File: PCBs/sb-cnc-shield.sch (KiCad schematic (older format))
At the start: 68 parts, among them J8 display, P1 XMOT, P10 power switch, P2 YMOT, P3 ZMOT, P4 AMOT, P5 UART, P6 I2C, P7 E_STOP, P8 12V-36V, Q0 IRF630, SW1 RESET, U1 ARDUINO_UNO_SHIELD, U2 X, U3 Y, U4 Z, U5 A

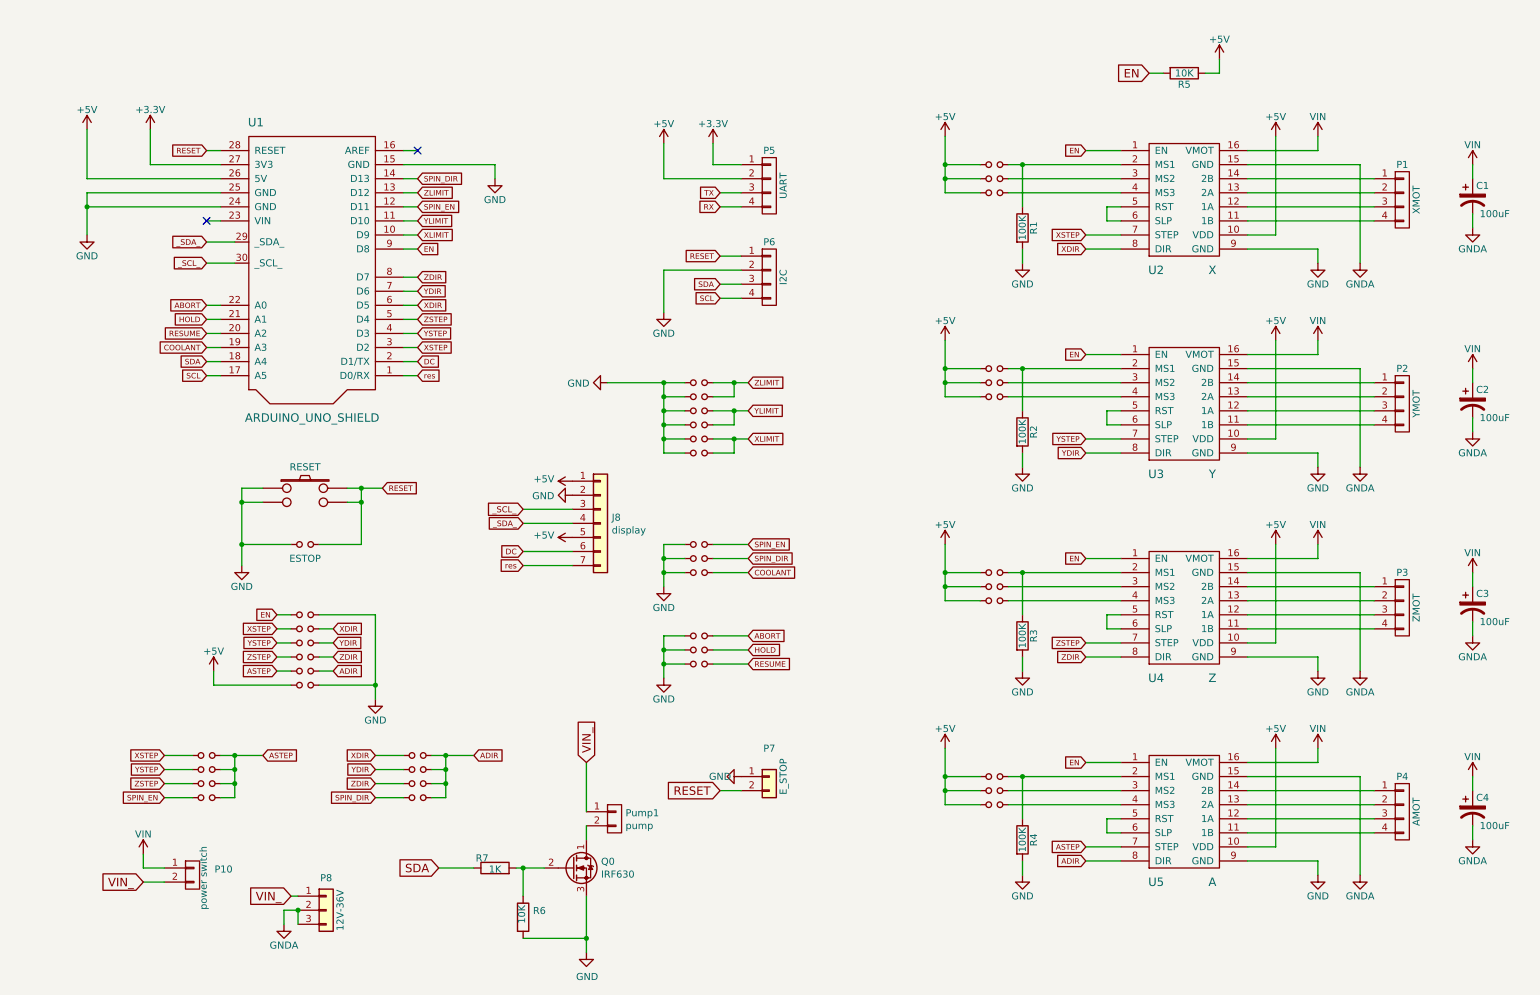
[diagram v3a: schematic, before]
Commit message: add voltage regulator shield for 5V rpi
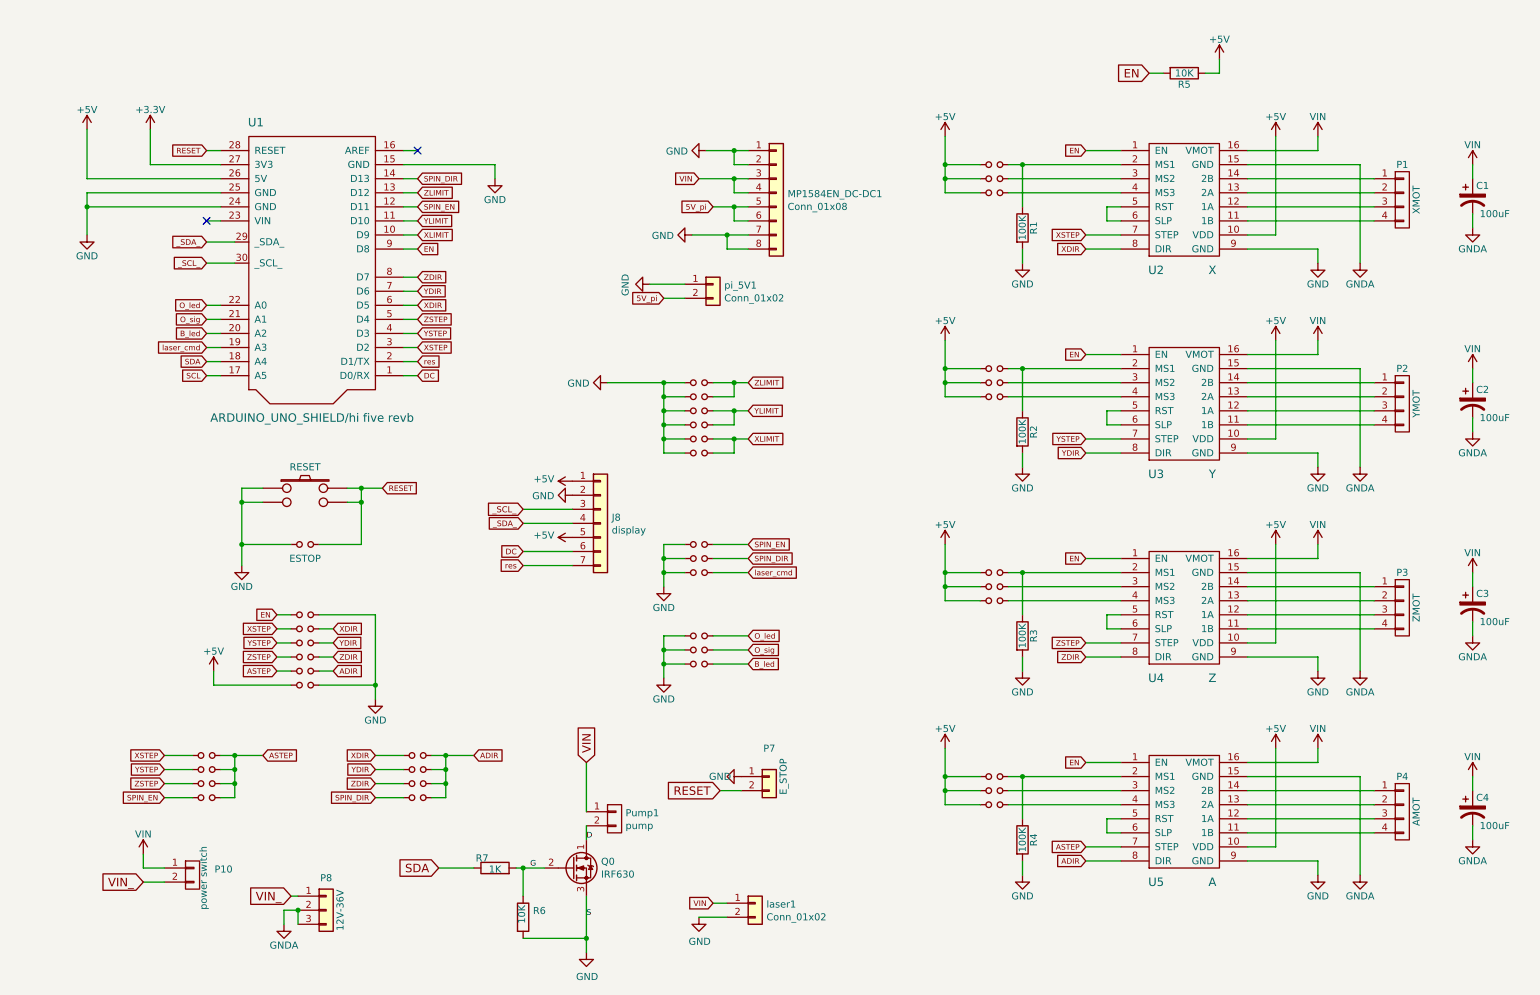
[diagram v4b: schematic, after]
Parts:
- removed P5: UART, Pin_Headers:Pin_Header_Straight_1x04, symbol sb-cnc-shield-rescue:CONN_01X04
- removed P6: I2C, Pin_Headers:Pin_Header_Straight_1x04, symbol sb-cnc-shield-rescue:CONN_01X04
- added MP1584EN_DC-DC1: Conn_01x08, pnp_box:MP1584EN convertisseur DC-DC, symbol Connector_Generic:Conn_01x08
- added laser1: Conn_01x02, Connector_PinHeader_2.54mm:PinHeader_1x02_P2.54mm_Vertical, symbol Connector_Generic:Conn_01x02
- added pi_5V1: Conn_01x02, Connector_JST:JST_EH_S2B-EH_1x02_P2.50mm_Horizontal, symbol Connector_Generic:Conn_01x02
- J8: footprint (none) -> Connector_PinHeader_2.54mm:PinHeader_1x07_P2.54mm_Vertical
- JP21: value CoolEn -> laser_cmd
- JP22: value Abort -> O_led
- JP23: value Hold -> O_sig
- JP24: value Resume -> B_led
- P1, P2, P3, P4: footprint Pin_Headers:Pin_Header_Straight_2x04 -> Connector_PinHeader_2.54mm:PinHeader_1x04_P2.54mm_Vertical
- U1: value ARDUINO_UNO_SHIELD -> ARDUINO_UNO_SHIELD/hi five revb
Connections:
- net DC: now also U1.1 (D0/RX); no longer U1.2 (D1/TX)
- net GND: now also MP1584EN_DC-DC1.1 (Pin_1), MP1584EN_DC-DC1.2 (Pin_2), MP1584EN_DC-DC1.7 (Pin_7), MP1584EN_DC-DC1.8 (Pin_8), laser1.2 (Pin_2), pi_5V1.1 (Pin_1)
- net VIN: now also Pump1.1 (P1), MP1584EN_DC-DC1.3 (Pin_3), MP1584EN_DC-DC1.4 (Pin_4), laser1.1 (Pin_1)
- net VIN_: no longer Pump1.1 (P1)
- net res: now also U1.2 (D1/TX); no longer U1.1 (D0/RX)
- net D: now reaches Pump1.2 (P2), Q0.1 (D)
- net G: now reaches Q0.2 (G), R6.1, R7.2
- net ABORT renamed O_led
- net COOLANT renamed laser_cmd
- net HOLD renamed O_sig
- net RESUME renamed B_led
- new net 5V_pi: MP1584EN_DC-DC1.5 (Pin_5), MP1584EN_DC-DC1.6 (Pin_6), pi_5V1.2 (Pin_2)

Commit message: modify kicad and create gerbers then ordering PCBs on JLPCB
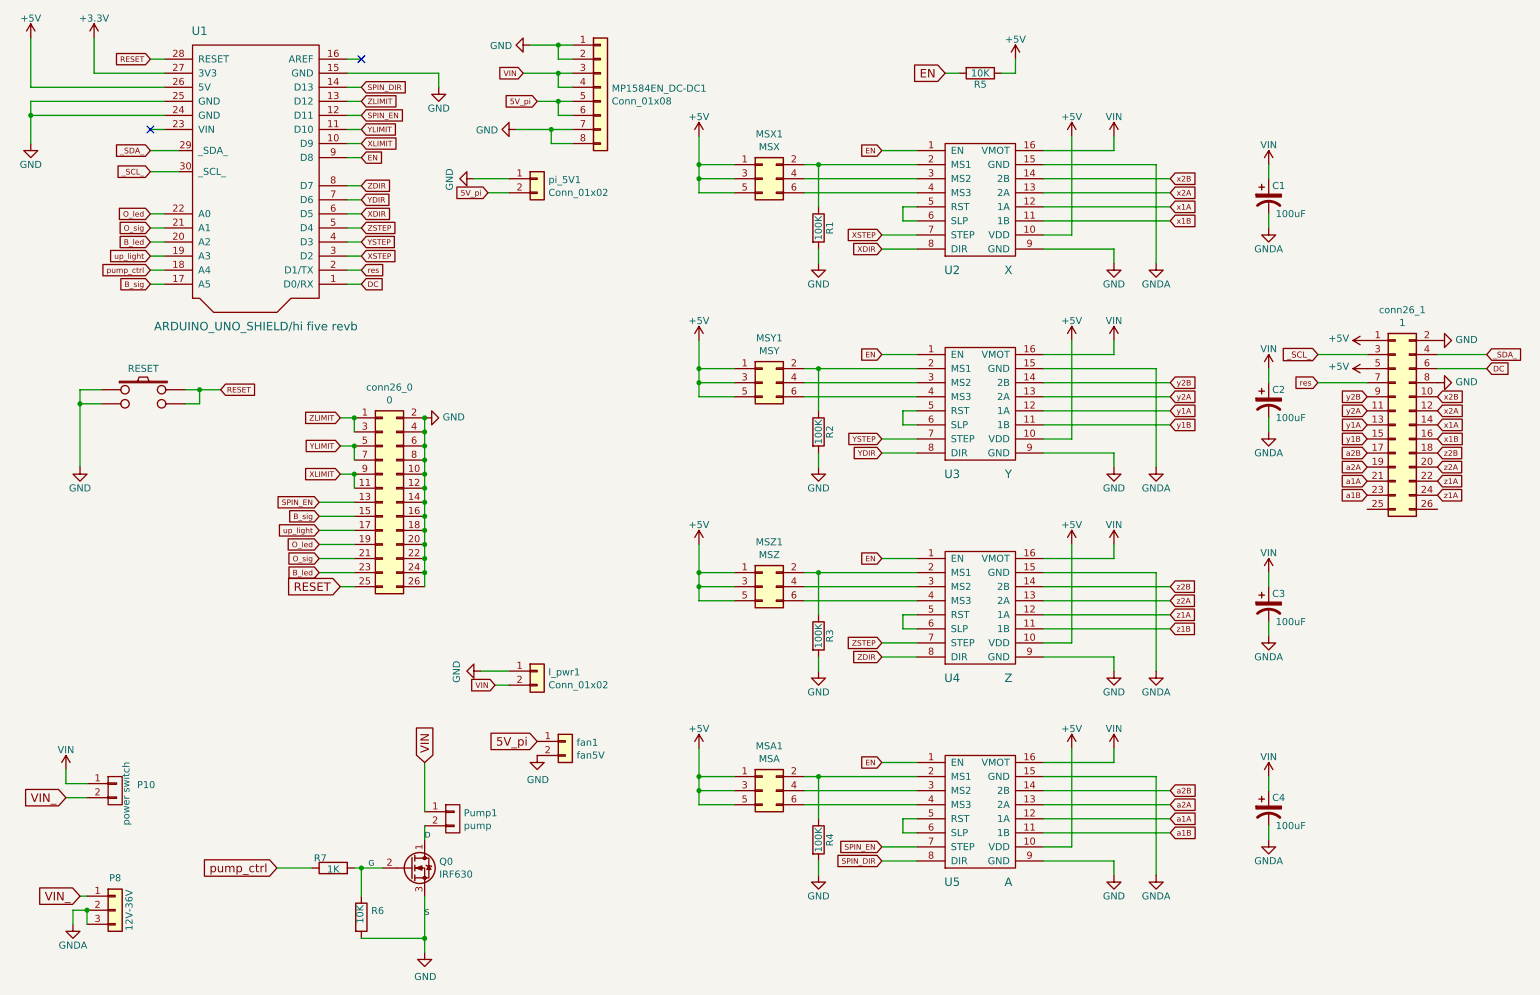
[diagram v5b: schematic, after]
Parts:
- removed J8: display, Connector_PinHeader_2.54mm:PinHeader_1x07_P2.54mm_Vertical, symbol Connector_Generic:Conn_01x07
- removed JP1, JP10, JP11, JP12, JP2, JP3, JP32, JP33, JP34, JP35, JP36, JP37, JP38, JP39, JP4, JP5, JP6, JP7, JP8, JP9: Jumper_NO_Small, footprints:Pin_100mil_Header_Straight_1x02, symbol Device:Jumper_NO_Small
- removed JP13: Z+, footprints:Pin_100mil_Header_Straight_1x02, symbol Device:Jumper_NO_Small
- removed JP14: Z-, footprints:Pin_100mil_Header_Straight_1x02, symbol Device:Jumper_NO_Small
- removed JP15: Y+, footprints:Pin_100mil_Header_Straight_1x02, symbol Device:Jumper_NO_Small
- removed JP16: Y-, footprints:Pin_100mil_Header_Straight_1x02, symbol Device:Jumper_NO_Small
- removed JP17: X+, footprints:Pin_100mil_Header_Straight_1x02, symbol Device:Jumper_NO_Small
- removed JP18: X-, footprints:Pin_100mil_Header_Straight_1x02, symbol Device:Jumper_NO_Small
- removed JP19: SpinEn, footprints:Pin_100mil_Header_Straight_1x02, symbol Device:Jumper_NO_Small
- removed JP20: SpinDir, footprints:Pin_100mil_Header_Straight_1x02, symbol Device:Jumper_NO_Small
- removed JP21: laser_cmd, footprints:Pin_100mil_Header_Straight_1x02, symbol Device:Jumper_NO_Small
- removed JP22: O_led, footprints:Pin_100mil_Header_Straight_1x02, symbol Device:Jumper_NO_Small
- removed JP23: O_sig, footprints:Pin_100mil_Header_Straight_1x02, symbol Device:Jumper_NO_Small
- removed JP24: B_led, footprints:Pin_100mil_Header_Straight_1x02, symbol Device:Jumper_NO_Small
- removed JP25: ESTOP, footprints:Pin_100mil_Header_Straight_1x02, symbol Device:Jumper_NO_Small
- removed JP26: EN/GND, footprints:Pin_100mil_Header_Straight_1x02, symbol Device:Jumper_NO_Small
- removed JP27: XSTEP/DIR, footprints:Pin_100mil_Header_Straight_1x02, symbol Device:Jumper_NO_Small
- removed JP28: YSTEP/DIR, footprints:Pin_100mil_Header_Straight_1x02, symbol Device:Jumper_NO_Small
- removed JP29: ZSTEP/DIR, footprints:Pin_100mil_Header_Straight_1x02, symbol Device:Jumper_NO_Small
- removed JP30: ASTEP/DIR, footprints:Pin_100mil_Header_Straight_1x02, symbol Device:Jumper_NO_Small
- removed JP31: +5V/GND, footprints:Pin_100mil_Header_Straight_1x02, symbol Device:Jumper_NO_Small
- removed P1: XMOT, Connector_PinHeader_2.54mm:PinHeader_1x04_P2.54mm_Vertical, symbol sb-cnc-shield-rescue:CONN_01X04
- removed P2: YMOT, Connector_PinHeader_2.54mm:PinHeader_1x04_P2.54mm_Vertical, symbol sb-cnc-shield-rescue:CONN_01X04
- removed P3: ZMOT, Connector_PinHeader_2.54mm:PinHeader_1x04_P2.54mm_Vertical, symbol sb-cnc-shield-rescue:CONN_01X04
- removed P4: AMOT, Connector_PinHeader_2.54mm:PinHeader_1x04_P2.54mm_Vertical, symbol sb-cnc-shield-rescue:CONN_01X04
- removed P7: E_STOP, Connector_PinHeader_2.54mm:PinHeader_1x02_P2.54mm_Vertical, symbol Connector_Generic:Conn_01x02
- added MSA1: MSA, Connector_PinHeader_2.54mm:PinHeader_2x03_P2.54mm_Vertical, symbol Connector_Generic:Conn_02x03_Odd_Even
- added MSX1: MSX, Connector_PinHeader_2.54mm:PinHeader_2x03_P2.54mm_Vertical, symbol Connector_Generic:Conn_02x03_Odd_Even
- added MSY1: MSY, Connector_PinHeader_2.54mm:PinHeader_2x03_P2.54mm_Vertical, symbol Connector_Generic:Conn_02x03_Odd_Even
- added MSZ1: MSZ, Connector_PinHeader_2.54mm:PinHeader_2x03_P2.54mm_Vertical, symbol Connector_Generic:Conn_02x03_Odd_Even
- added conn26_0: 0, Connector_IDC:IDC-Header_2x13_P2.54mm_Vertical, symbol Connector_Generic:Conn_02x13_Odd_Even
- added conn26_1: 1, Connector_IDC:IDC-Header_2x13_P2.54mm_Vertical, symbol Connector_Generic:Conn_02x13_Odd_Even
- added fan1: fan5V, Connector_JST:JST_SH_BM02B-SRSS-TB_1x02-1MP_P1.00mm_Vertical, symbol Connector_Generic:Conn_01x02
- Pump1: footprint Connector_PinHeader_2.54mm:PinHeader_1x02_P2.54mm_Vertical -> Connector_JST:JST_EH_B2B-EH-A_1x02_P2.50mm_Vertical
- l_pwr1: renamed from laser1; footprint Connector_PinHeader_2.54mm:PinHeader_1x02_P2.54mm_Vertical -> Connector_JST:JST_EH_B2B-EH-A_1x02_P2.50mm_Vertical
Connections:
- net ADIR is gone; now on net SPIN_DIR: U5.8 (DIR)
- net ASTEP is gone; now on net SPIN_EN: U5.7 (STEP)
- net +5V: now also MSA1.1 (Pin_1), MSA1.3 (Pin_3), MSA1.5 (Pin_5), MSX1.1 (Pin_1), MSX1.3 (Pin_3), MSX1.5 (Pin_5), MSY1.1 (Pin_1), MSY1.3 (Pin_3), MSY1.5 (Pin_5), MSZ1.1 (Pin_1), MSZ1.3 (Pin_3), MSZ1.5 (Pin_5), conn26_1.1 (Pin_1), conn26_1.5 (Pin_5)
- net 5V_pi: now also fan1.1 (Pin_1)
- net B_led: now also conn26_0.23 (Pin_23)
- net DC: now also conn26_1.6 (Pin_6)
- net GND: now also l_pwr1.1 (Pin_1), conn26_0.10 (Pin_10), conn26_0.12 (Pin_12), conn26_0.14 (Pin_14), conn26_0.16 (Pin_16), conn26_0.18 (Pin_18), conn26_0.2 (Pin_2), conn26_0.20 (Pin_20), conn26_0.22 (Pin_22), conn26_0.24 (Pin_24), conn26_0.26 (Pin_26), conn26_0.4 (Pin_4), conn26_0.6 (Pin_6), conn26_0.8 (Pin_8), conn26_1.2 (Pin_2), conn26_1.8 (Pin_8), fan1.2 (Pin_2); no longer l_pwr1.2 (Pin_2)
- net O_led: now also conn26_0.19 (Pin_19)
- net O_sig: now also conn26_0.21 (Pin_21)
- net RESET: now also conn26_0.25 (Pin_25)
- net SPIN_EN: now also conn26_0.13 (Pin_13)
- net VIN: now also l_pwr1.2 (Pin_2); no longer l_pwr1.1 (Pin_1)
- net XLIMIT: now also conn26_0.11 (Pin_11), conn26_0.9 (Pin_9)
- net YLIMIT: now also conn26_0.5 (Pin_5), conn26_0.7 (Pin_7)
- net ZLIMIT: now also conn26_0.1 (Pin_1), conn26_0.3 (Pin_3)
- net _SCL_: now also conn26_1.3 (Pin_3)
- net _SDA_: now also conn26_1.4 (Pin_4)
- net res: now also conn26_1.7 (Pin_7)
- net a1B: now reaches U5.11 (1B)
- net a1B: now also conn26_1.23 (Pin_23)
- net a1A: now reaches U5.12 (1A)
- net a1A: now also conn26_1.21 (Pin_21)
- net a2A: now reaches U5.13 (2A)
- net a2A: now also conn26_1.19 (Pin_19)
- net a2B: now reaches U5.14 (2B)
- net a2B: now also conn26_1.17 (Pin_17)
- net at R4.1, U5.2 (MS1): now also MSA1.2 (Pin_2)
- net at U5.3 (MS2): now also MSA1.4 (Pin_4)
- net at U5.4 (MS3): now also MSA1.6 (Pin_6)
- net y1B: now reaches U3.11 (1B)
- net y1B: now also conn26_1.15 (Pin_15)
- net y1A: now reaches U3.12 (1A)
- net y1A: now also conn26_1.13 (Pin_13)
- net y2A: now reaches U3.13 (2A)
- net y2A: now also conn26_1.11 (Pin_11)
- net y2B: now reaches U3.14 (2B)
- net y2B: now also conn26_1.9 (Pin_9)
- net at R2.1, U3.2 (MS1): now also MSY1.2 (Pin_2)
- net at U3.3 (MS2): now also MSY1.4 (Pin_4)
- net at U3.4 (MS3): now also MSY1.6 (Pin_6)
- net x1B: now reaches U2.11 (1B)
- net x1B: now also conn26_1.16 (Pin_16)
- net x1A: now reaches U2.12 (1A)
- net x1A: now also conn26_1.14 (Pin_14)
- net x2A: now reaches U2.13 (2A)
- net x2A: now also conn26_1.12 (Pin_12)
- net x2B: now reaches U2.14 (2B)
- net x2B: now also conn26_1.10 (Pin_10)
- net at R1.1, U2.2 (MS1): now also MSX1.2 (Pin_2)
- net at U2.3 (MS2): now also MSX1.4 (Pin_4)
- net at U2.4 (MS3): now also MSX1.6 (Pin_6)
- net z1B: now reaches U4.11 (1B)
- net z1A: now reaches U4.12 (1A)
- net z1A: now also conn26_1.22 (Pin_22), conn26_1.24 (Pin_24)
- net z2A: now reaches U4.13 (2A)
- net z2A: now also conn26_1.20 (Pin_20)
- net z2B: now reaches U4.14 (2B)
- net z2B: now also conn26_1.18 (Pin_18)
- net at R3.1, U4.2 (MS1): now also MSZ1.2 (Pin_2)
- net at U4.3 (MS2): now also MSZ1.4 (Pin_4)
- net at U4.4 (MS3): now also MSZ1.6 (Pin_6)
- net SCL renamed B_sig
- net B_sig: now also conn26_0.15 (Pin_15)
- net SDA renamed pump_ctrl
- net laser_cmd renamed up_light
- net up_light: now also conn26_0.17 (Pin_17)
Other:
- moved on the sheet: C1, C2, C3, C4, MP1584EN_DC-DC1, P10, P8, Pump1, Q0, R1, R2, R3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

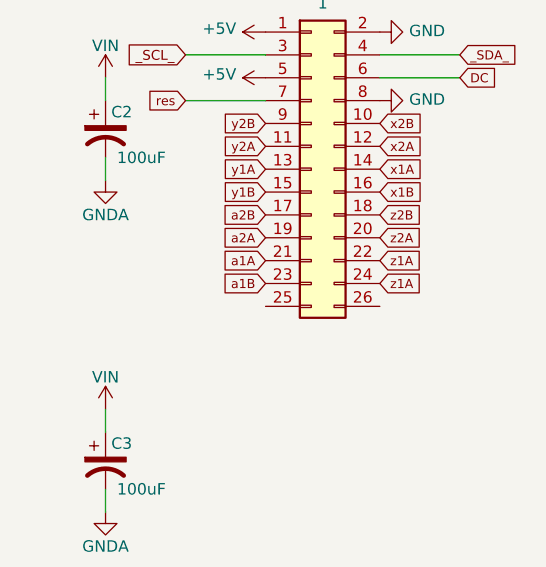
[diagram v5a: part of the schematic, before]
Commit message: correct z1A pinoutgit add .!
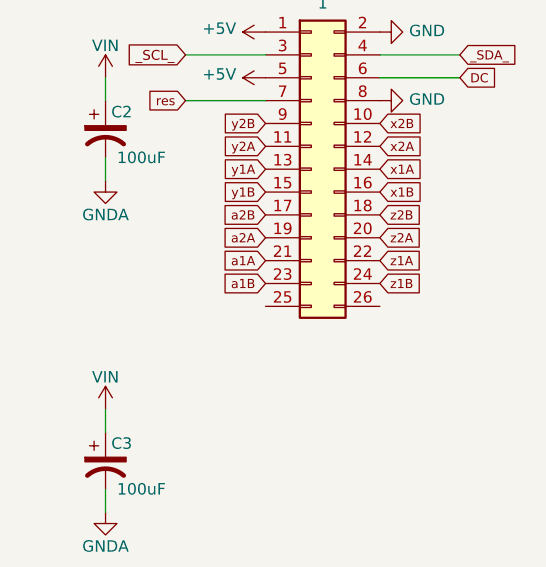
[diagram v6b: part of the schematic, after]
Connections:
- net z1A: no longer conn26_1.24 (Pin_24)
- net z1B: now also conn26_1.24 (Pin_24)
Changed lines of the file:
@@
 z1A
 Text GLabel 10600 4050 2    40   Input ~ 0
-z1A
+z1B
 Text GLabel 8700 6150 2    40   Input ~ 0
 a2B
